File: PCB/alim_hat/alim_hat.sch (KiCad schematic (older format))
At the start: 48 parts, among them J1 Screw_Terminal_01x04, J10 Conn_01x02, J11 Conn_01x02, J12 Conn_01x02, J13 Conn_01x02, J14 Conn_01x02, J15 Conn_01x02, J16 Conn_01x02, J2 Conn_01x02_Male, J3 Conn_02x04_Odd_Even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

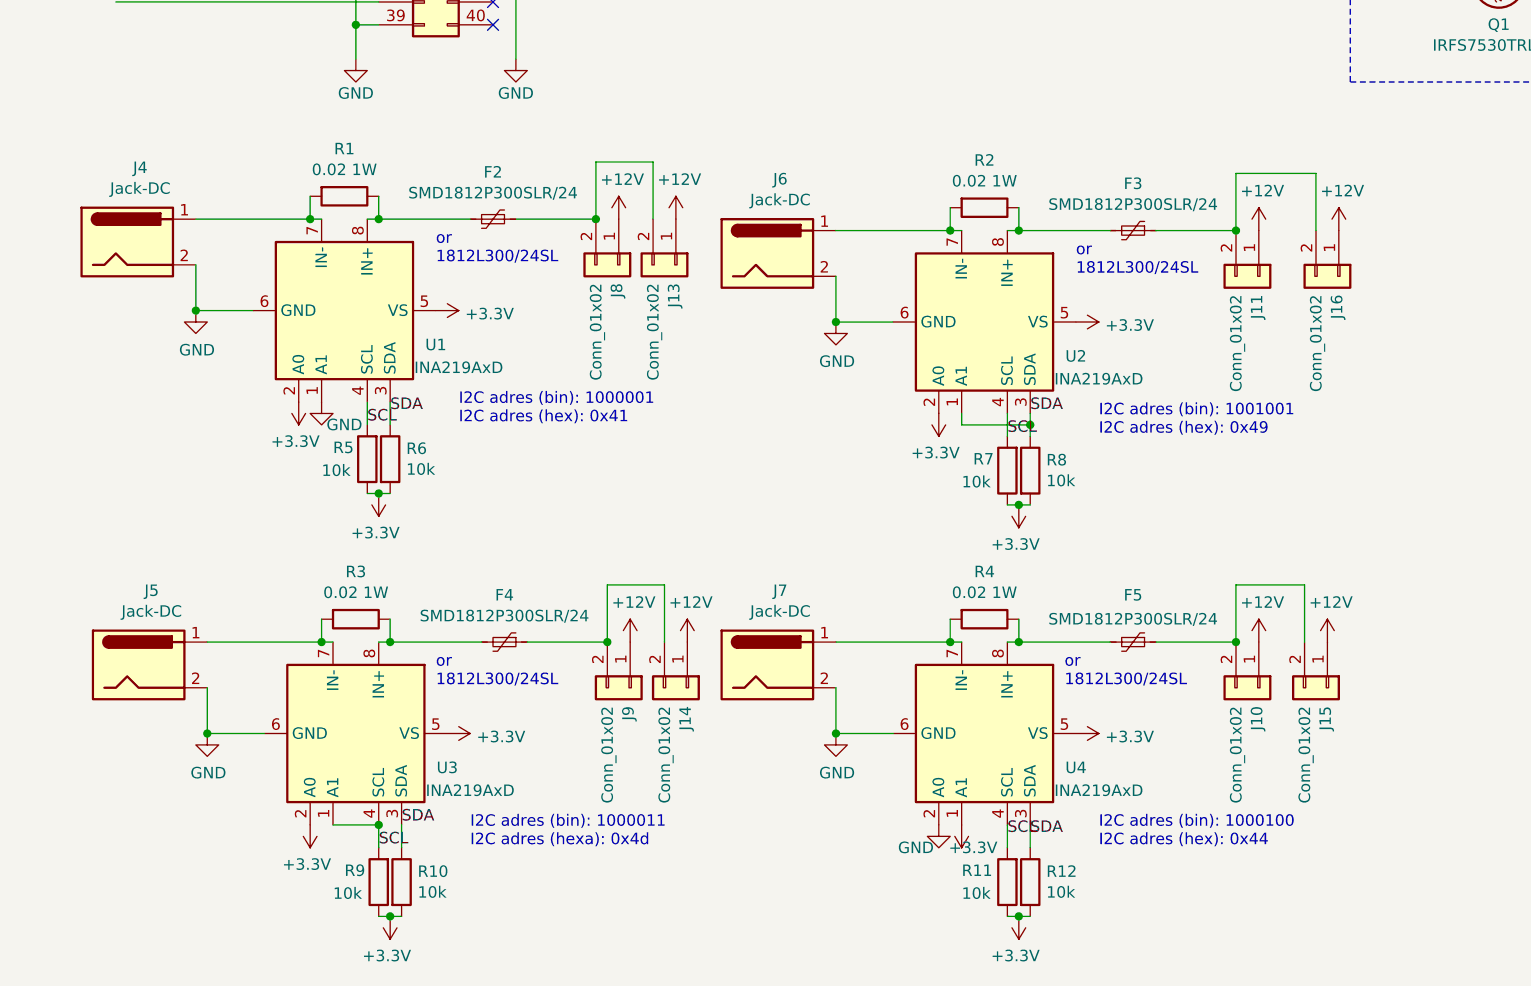
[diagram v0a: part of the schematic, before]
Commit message: change 12v to GND Jack DC cut-off
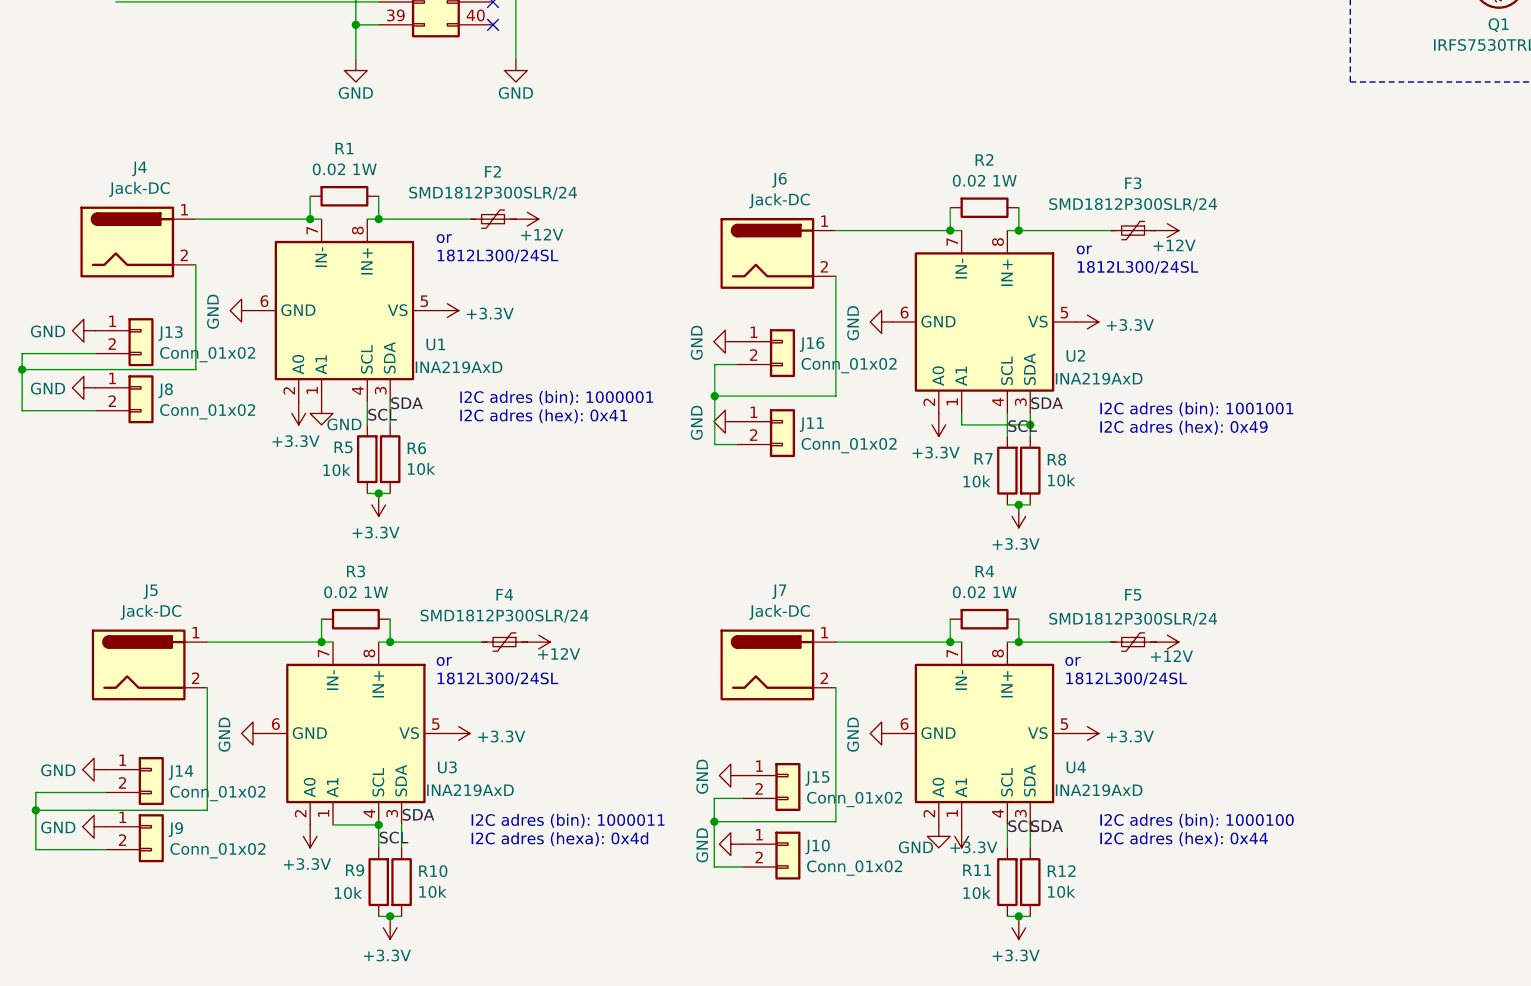
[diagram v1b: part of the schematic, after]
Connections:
- net +12V: now also F2.1, F3.1, F4.1, F5.1; no longer J10.1 (Pin_1), J11.1 (Pin_1), J13.1 (Pin_1), J14.1 (Pin_1), J15.1 (Pin_1), J16.1 (Pin_1), J8.1 (Pin_1), J9.1 (Pin_1)
- net GND: now also J10.1 (Pin_1), J11.1 (Pin_1), J13.1 (Pin_1), J14.1 (Pin_1), J15.1 (Pin_1), J16.1 (Pin_1), J8.1 (Pin_1), J9.1 (Pin_1); no longer J4.2, J5.2, J6.2, J7.2
- net at J14.2 (Pin_2), J9.2 (Pin_2): now also J5.2; no longer F4.1
- net at J13.2 (Pin_2), J8.2 (Pin_2): now also J4.2; no longer F2.1
- net at J10.2 (Pin_2), J15.2 (Pin_2): now also J7.2; no longer F5.1
- net at J11.2 (Pin_2), J16.2 (Pin_2): now also J6.2; no longer F3.1
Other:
- moved on the sheet: J10, J11, J13, J14, J15, J16, J8, J9

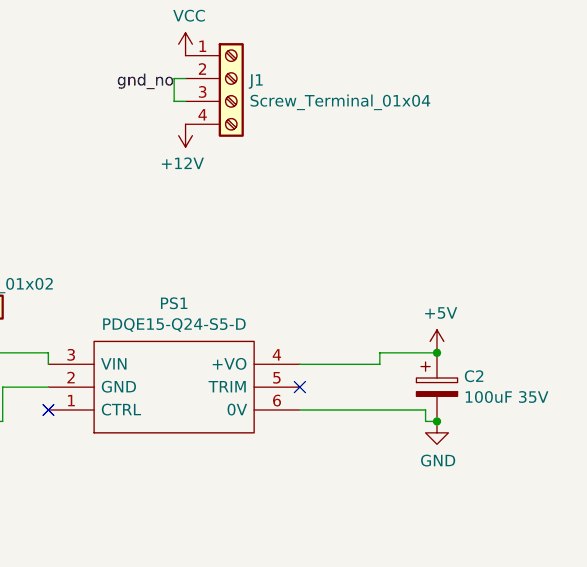
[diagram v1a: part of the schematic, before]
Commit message: add pin header for inject 5V in VCC
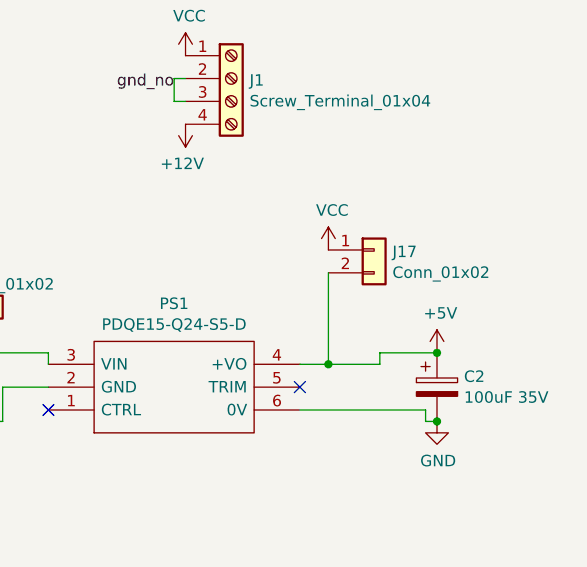
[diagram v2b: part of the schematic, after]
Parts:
- added J17: Conn_01x02, Connector_PinHeader_2.54mm:PinHeader_1x02_P2.54mm_Vertical, symbol Connector_Generic:Conn_01x02
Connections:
- net +5V: now also J17.2 (Pin_2)
- net VCC: now also J17.1 (Pin_1)
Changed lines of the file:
@@
 Connection ~ 8100 5700
 Wire Wire Line
-	9950 5450 10300 5450
+	9950 5450 10075 5450
 Wire Wire Line
 	10300 5450 10300 5400
@@
 $EndComp
 $Comp
-L power:GND #PWR?
+L power:GND #PWR0115
 U 1 1 608906F9
 P 3990 6584
-F 0 "#PWR?" H 3990 6334 50  0001 C CNN
+F 0 "#PWR0115" H 3990 6334 50  0001 C CNN
 F 1 "GND" H 3995 6411 50  0000 C CNN
 F 2 "" H 3990 6584 50  0001 C CNN
@@
 $EndComp
 $Comp
-L power:GND #PWR?
+L power:GND #PWR0141
 U 1 1 608912E4
 P 3990 6284
-F 0 "#PWR?" H 3990 6034 50  0001 C CNN
+F 0 "#PWR0141" H 3990 6034 50  0001 C CNN
 F 1 "GND" H 3995 6111 50  0000 C CNN
 F 2 "" H 3990 6284 50  0001 C CNN
@@
 	3870 4486 3966 4486
 $Comp
-L power:GND #PWR?
+L power:GND #PWR0142
 U 1 1 608D9114
 P 3966 4736
-F 0 "#PWR?" H 3966 4486 50  0001 C CNN
+F 0 "#PWR0142" H 3966 4486 50  0001 C CNN
 F 1 "GND" H 3971 4563 50  0000 C CNN
 F 2 "" H 3966 4736 50  0001 C CNN
@@
 $EndComp
 $Comp
-L power:GND #PWR?
+L power:GND #PWR0143
 U 1 1 608D9DC4
 P 3966 4386
-F 0 "#PWR?" H 3966 4136 50  0001 C CNN
+F 0 "#PWR0143" H 3966 4136 50  0001 C CNN
 F 1 "GND" H 3971 4213 50  0000 C CNN
 F 2 "" H 3966 4386 50  0001 C CNN
@@
 	3868 6486 3868 6384
 $Comp
-L power:GND #PWR?
+L power:GND #PWR0144
 U 1 1 609AAB1E
 P 1205 6258
-F 0 "#PWR?" H 1205 6008 50  0001 C CNN
+F 0 "#PWR0144" H 1205 6008 50  0001 C CNN
 F 1 "GND" V 1210 6130 50  0000 R CNN
 F 2 "" H 1205 6258 50  0001 C CNN
@@
 $EndComp
 $Comp
-L power:GND #PWR?
+L power:GND #PWR0145
 U 1 1 609AB316
 P 1205 6508
-F 0 "#PWR?" H 1205 6258 50  0001 C CNN
+F 0 "#PWR0145" H 1205 6258 50  0001 C CNN
 F 1 "GND" V 1210 6380 50  0000 R CNN
 F 2 "" H 1205 6508 50  0001 C CNN
@@
 $EndComp
 $Comp
-L power:GND #PWR?
+L power:GND #PWR0146
 U 1 1 609ACD61
 P 1160 4338
-F 0 "#PWR?" H 1160 4088 50  0001 C CNN
+F 0 "#PWR0146" H 1160 4088 50  0001 C CNN
 F 1 "GND" V 1165 4210 50  0000 R CNN
 F 2 "" H 1160 4338 50  0001 C CNN
@@
 $EndComp
 $Comp
-L power:GND #PWR?
+L power:GND #PWR0147
 U 1 1 609AD2AD
 P 1160 4588
-F 0 "#PWR?" H 1160 4338 50  0001 C CNN
+F 0 "#PWR0147" H 1160 4338 50  0001 C CNN
 F 1 "GND" V 1165 4460 50  0000 R CNN
 F 2 "" H 1160 4588 50  0001 C CNN
@@
 Wire Wire Line
 	900  6436 900  6608
+$Comp
+L Connector_Generic:Conn_01x02 J17
+U 1 1 6087D32D
+P 10275 4950
+F 0 "J17" H 10355 4942 50  0000 L CNN
+F 1 "Conn_01x02" H 10355 4851 50  0000 L CNN
+F 2 "Connector_PinHeader_2.54mm:PinHeader_1x02_P2.54mm_Vertical" H 10275 4950 50  0001 C CNN
+F 3 "~" H 10275 4950 50  0001 C CNN
+	1    10275 4950
+	1    0    0    -1
+$EndComp
+Wire Wire Line
+	10075 5050 10075 5450
+Connection ~ 10075 5450
+Wire Wire Line
+	10075 5450 10300 5450
+$Comp
+L power:VCC #PWR0148
+U 1 1 60886F00
+P 10075 4950
+F 0 "#PWR0148" H 10075 4800 50  0001 C CNN
+F 1 "VCC" H 10092 5123 50  0000 C CNN
+F 2 "" H 10075 4950 50  0001 C CNN
+F 3 "" H 10075 4950 50  0001 C CNN
+	1    10075 4950
+	1    0    0    -1
+$EndComp
 $EndSCHEMATC

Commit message: change trace for CP capa
help jlcpcb analyse
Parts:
- C1, C2: footprint capa:CAPAE660X800N -> Capacitor_SMD:CP_Elec_6.3x7.7
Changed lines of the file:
@@
 F 0 "C1" H 8218 5596 50  0000 L CNN
 F 1 "100uF 35V" H 8218 5505 50  0000 L CNN
-F 2 "capa:CAPAE660X800N" H 8138 5400 50  0001 C CNN
+F 2 "Capacitor_SMD:CP_Elec_6.3x7.7" H 8138 5400 50  0001 C CNN
 F 3 "~" H 8100 5550 50  0001 C CNN
 F 4 "C134792" H 8100 5550 50  0001 C CNN "LCSC"
@@
 F 0 "C2" H 10668 5596 50  0000 L CNN
 F 1 "100uF 35V" H 10668 5505 50  0000 L CNN
-F 2 "capa:CAPAE660X800N" H 10588 5400 50  0001 C CNN
+F 2 "Capacitor_SMD:CP_Elec_6.3x7.7" H 10588 5400 50  0001 C CNN
 F 3 "~" H 10550 5550 50  0001 C CNN
 F 4 "C134792" H 10550 5550 50  0001 C CNN "LCSC"
